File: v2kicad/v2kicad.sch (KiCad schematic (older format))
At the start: 3 parts

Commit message: Progress
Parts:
- BT1: footprint xxx:CR2032-white-smd -> sydcon-badges-2016:CR2032-white-smd (1)
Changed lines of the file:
@@
 LIBS:contrib
 LIBS:valves
+LIBS:v2kicad-cache
 EELAYER 25 0
 EELAYER END
@@
 F 0 "BT1" H 6850 3225 50  0000 L CNN
 F 1 "Battery" H 6850 3125 50  0000 L CNN
-F 2 "xxx:CR2032-white-smd" H 7600 3125 50  0000 C CNN
+F 2 "sydcon-badges-2016:CR2032-white-smd (1)" H 7950 3200 50  0000 C CNN
 F 3 "" V 6750 3215 50  0000 C CNN
 	1    6750 3175

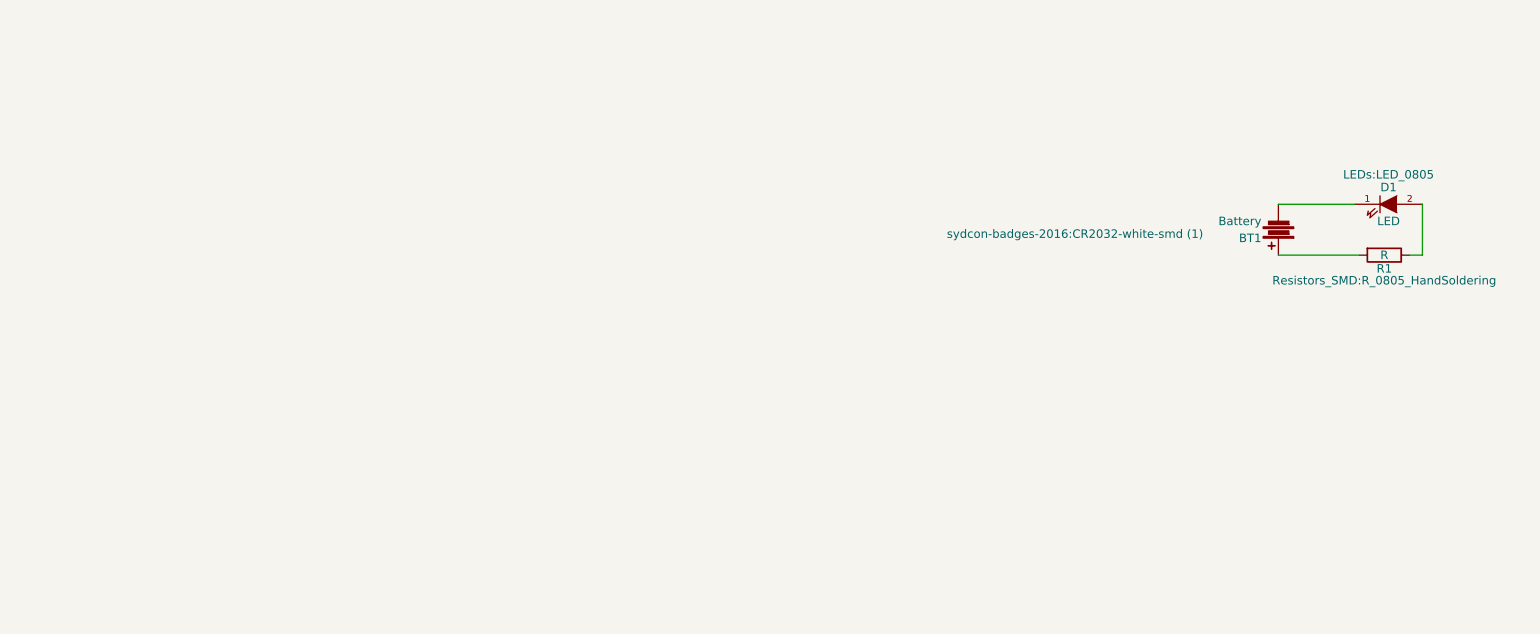
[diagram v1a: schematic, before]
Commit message: Redone traces for main LED to avoid silkscreen
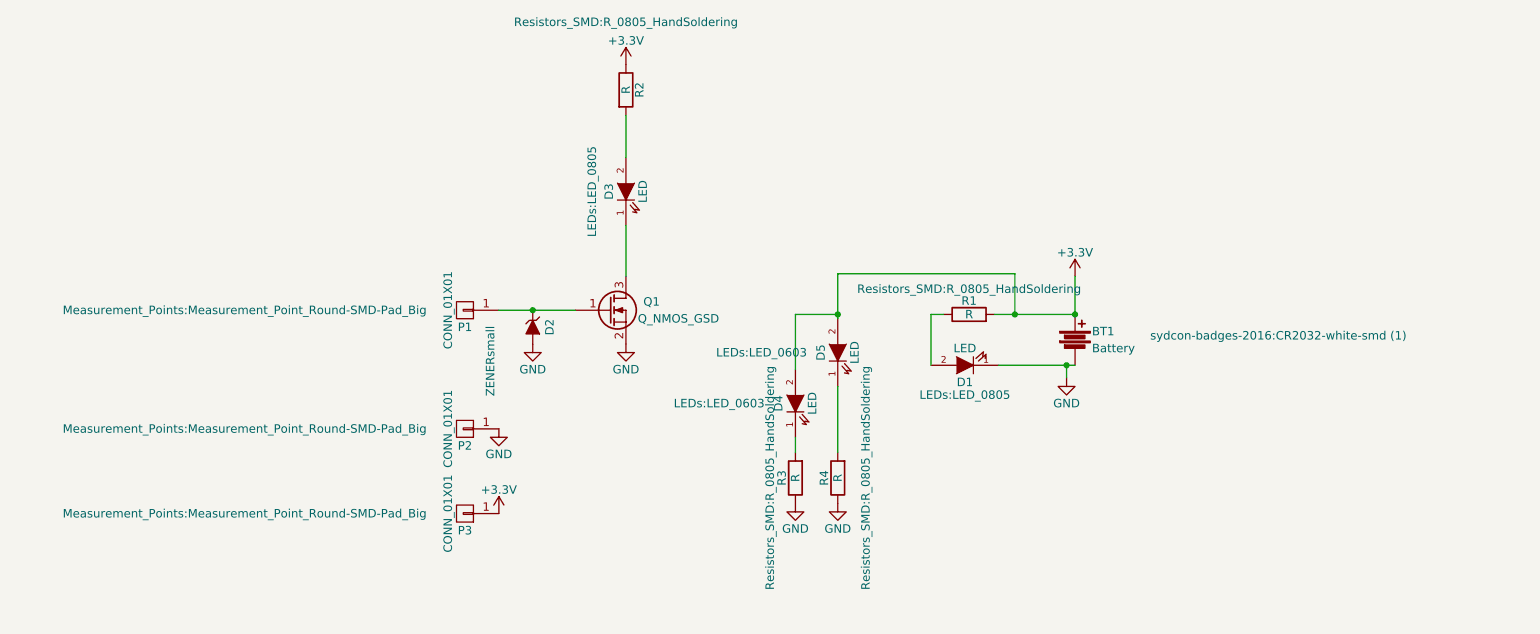
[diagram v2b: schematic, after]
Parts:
- added D2: ZENERsmall, Diodes_SMD:SMA-SMB_Universal_Handsoldering, symbol ZENERsmall
- added D3: LED, LEDs:LED_0805, symbol LED
- added D4, D5: LED, LEDs:LED_0603, symbol LED
- added P1, P2, P3: CONN_01X01, Measurement_Points:Measurement_Point_Round-SMD-Pad_Big, symbol CONN_01X01
- added Q1: Q_NMOS_GSD, TO_SOT_Packages_SMD:SOT-23_Handsoldering, symbol Q_NMOS_GSD
- added R2, R3, R4: R, Resistors_SMD:R_0805_HandSoldering, symbol R
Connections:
- net GND: now reaches BT1.2, D1.1 (K)
- net GND: now also D2.2 (A), P2.1 (P1), Q1.2 (S), R3.1, R4.1
- net +3V3: now reaches BT1.1, R1.2
- net +3V3: now also D4.2 (A), D5.2 (A), P3.1 (P1), R2.1
- new net: D2.1 (K), P1.1 (P1), Q1.1 (G)
- new net: D3.1 (K), Q1.3 (D)
- new net: D3.2 (A), R2.2
- new net: D5.1 (K), R4.2
- new net: D4.1 (K), R3.2
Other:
- moved on the sheet: BT1, D1, R1
